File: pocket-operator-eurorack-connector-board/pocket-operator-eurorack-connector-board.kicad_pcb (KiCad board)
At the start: 2 copper layers, 14.4 x 88.9 mm, 6 parts, among them J1 Conn_02x04_Odd_Even, J2 AudioJack2_SwitchT, J3 AudioJack2_SwitchT, J4 AudioJack2_SwitchT, J5 AudioJack2_SwitchT, SW1 SW_Push_SPDT

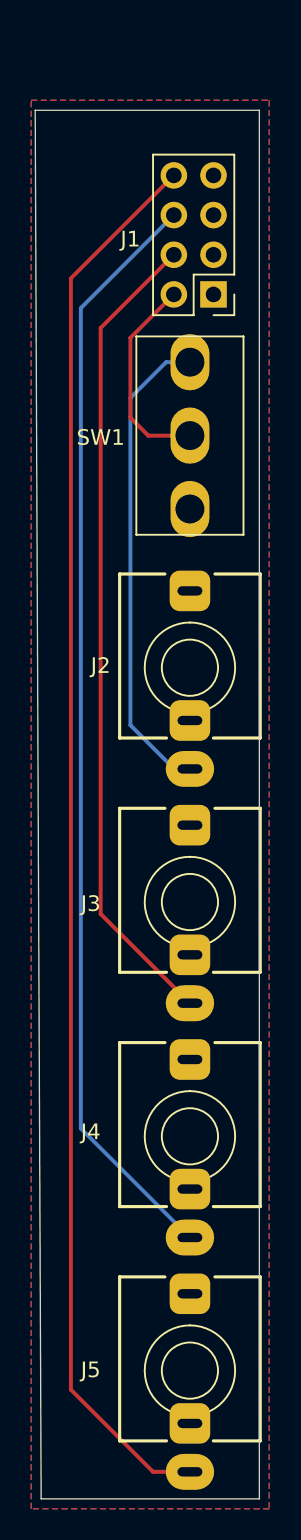
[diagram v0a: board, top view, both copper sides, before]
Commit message: connector board finalised, ready for review
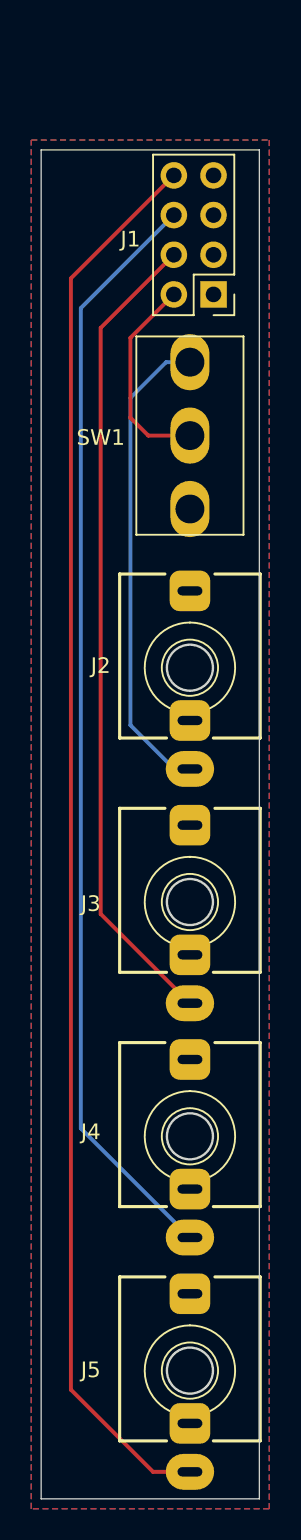
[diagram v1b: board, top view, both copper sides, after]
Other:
- board size 14.4 x 88.9 mm -> 14 x 86.4 mm

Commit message: finished and gerbers sent off for production
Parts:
- added G***: LOGO, pocket-operator-eurorack_lib:logo_small, B.Cu at (-5.71, 85.1)
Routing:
- net /OUT_R: track 90.3 -> 89.2 mm
- net /OUT_L: track 70.8 -> 70.3 mm
- net GND: vias 0 -> 19
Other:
- board text added: "Connector board for pocket operator eurorack by ric from ealing This won’t work without the main board, but you can try"
